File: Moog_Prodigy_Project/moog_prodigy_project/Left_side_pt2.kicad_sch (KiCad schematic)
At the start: 64 parts, among them J7 Conn_01x02_Socket, Q4 BC107, Q7 BC549, SW3 Switch_4x4, SW4 SW_Slide_DPDT_3x3, SW5 Switch_4x4, U2B2 OPA134, U4B1 OPA134, U6 NE5532, U7 AD8066ARM, U8 LT1011CN8

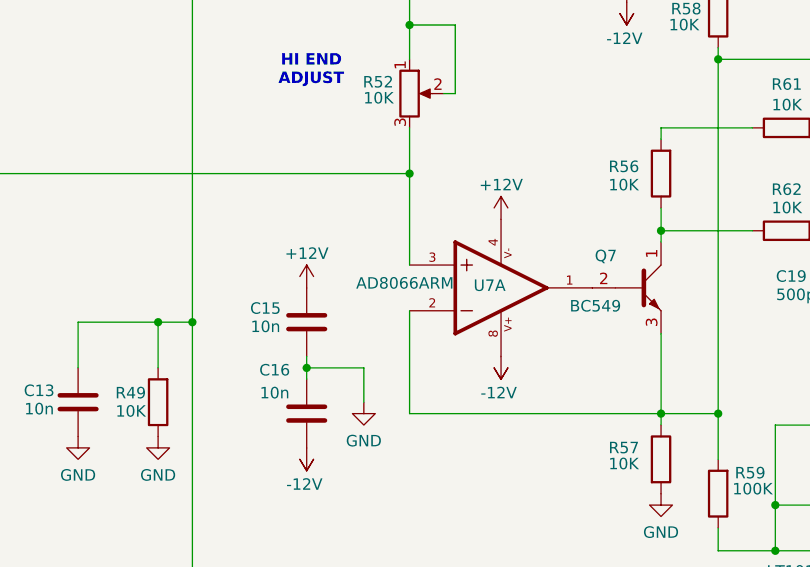
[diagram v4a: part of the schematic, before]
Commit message: SMD component to THT component update PCB
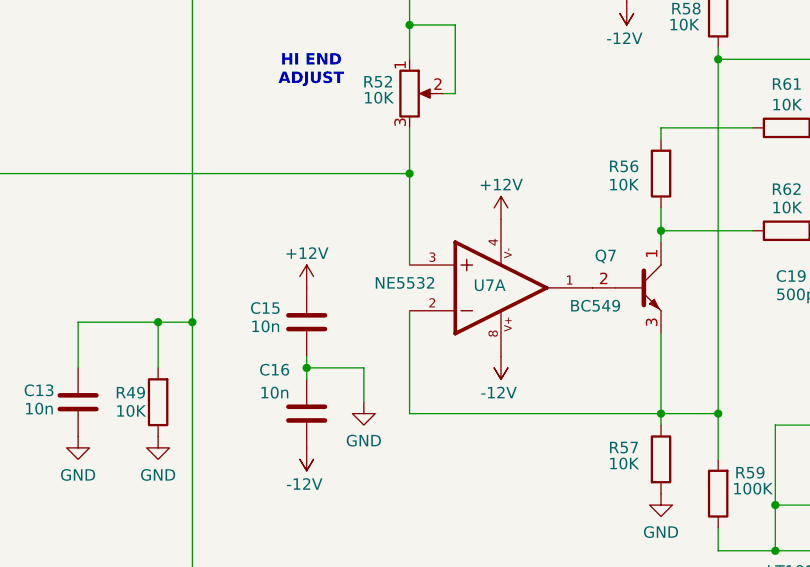
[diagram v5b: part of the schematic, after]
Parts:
- U7: value AD8066ARM -> NE5532; footprint Package_DIP:DIP-8_W7.62mm_Socket -> NE5532AP:DIP794W45P254L1016H508Q8
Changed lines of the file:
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@@
 			)
 		)
-		(property "Value" "AD8066ARM"
+		(property "Value" "NE5532"
 			(at 178.562 104.902 0)
 			(effects
@@
 			)
 		)
-		(property "Footprint" "Package_DIP:DIP-8_W7.62mm_Socket"
+		(property "Footprint" "NE5532AP:DIP794W45P254L1016H508Q8"
 			(at 189.23 105.41 0)
 			(effects

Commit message: Routhed PCB final 17.05.2026
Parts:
- Q5, Q6: footprint BF256C:TO92127P478H483-3 -> Package_TO_SOT_THT:TO-92_Inline
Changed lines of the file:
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@@
 			)
 		)
-		(property "Footprint" "BF256C:TO92127P478H483-3"
+		(property "Footprint" "Package_TO_SOT_THT:TO-92_Inline"
 			(at 184.15 58.42 0)
 			(effects
@@
 			)
 		)
-		(property "Footprint" "BF256C:TO92127P478H483-3"
+		(property "Footprint" "Package_TO_SOT_THT:TO-92_Inline"
 			(at 129.54 33.02 0)
 			(effects

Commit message: Fix 1 nakon review-a 27.05.2026
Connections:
- net +12V: now also CA3046_2.; no longer CA3046_2.8
- net -12V: now also Q4. (E); no longer Q4.1 (E)
- net GND: now also CA3046_2.; no longer CA3046_2.10, CA3046_2.6
- net at R37.2, U4B1.3 (+): now also CA3046_2.; no longer CA3046_2.9
- net at R33.2, R34.2, R35.1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: now also CA3046_2.; no longer CA3046_2.2
- net at C18.1, R54.1, R55.1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: now also Q6.; no longer Q6.2 (G)
- net at R57.1, R58.1, R59.2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: now also Q7. (E), U7.3 (+); no longer Q7.3 (E), U7.2
- net at R40.2, RV8.3: now also CA3046_2.; no longer CA3046_2.4
- net at C17.1, R52.1, R52.2: now also Q5., Q6.; no longer Q5.3 (S), Q6.1 (D)
- net at C17.2, R54.2, U6.1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: now also Q5., Q6.; no longer Q5.1 (D), Q6.3 (S)
- net at SW4.5 (B): now also Q5.; no longer Q5.2 (G)
- net at R56.1, R62.1: now also Q7. (E); no longer Q7.1 (C)
- net at R45.2, R47.2: now also Q4. (E); no longer Q4.2 (B)
- net at R42.2, R44.2: now also CA3046_2.; no longer CA3046_2.13
- net at C12.2, R43.2, SW3.5 (E)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: now also CA3046_2.; no longer CA3046_2.5
- net at U7.1: now also Q7. (E); no longer Q7.2 (B)
- net at R48.1: now also Q4. (E); no longer Q4.3 (C)
- net at R48.2: now also CA3046_2.; no longer CA3046_2.7
- net at C12.1, U2B2.6: now also CA3046_2.; no longer CA3046_2.3
- new net: CA3046_2., R52.3, U7.2 (-)
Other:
- title: (none) -> Drugi segment leve strane šeme
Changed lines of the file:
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@@
 	(generator_version "9.0")
 	(paper "A4")
+	(title_block
+		(title "Drugi segment leve strane šeme")
+		(date "27.05.2026")
+		(rev "Marjan Urekar")
+		(comment 1 "Fakultet tehničkih nauka")
+		(comment 2 "Univerzitet u Novom Sadu")
+		(comment 3 "Merno-Informacioni sistemi")
+		(comment 4 "Jovan Mastelica E1 105/2023")
+	)
 	(text "OSC 2\nFREQ TRIM"
 		(exclude_from_sim no)
@@
 	(wire
 		(pts
+			(xy 179.07 102.87) (xy 181.61 102.87)
+		)
+		(stroke
+			(width 0)
+			(type default)
+		)
+	)
+	(wire
+		(pts
 			(xy 77.47 71.12) (xy 85.09 71.12)
 		)
@@
 	(wire
 		(pts
-			(xy 242.57 137.16) (xy 245.11 137.16)
+			(xy 142.24 109.22) (xy 142.24 114.3)
 		)
 		(stroke
@@
 	(wire
 		(pts
-			(xy 142.24 109.22) (xy 142.24 114.3)
+			(xy 265.43 91.44) (xy 265.43 82.55)
 		)
 		(stroke
@@
 	(wire
 		(pts
-			(xy 265.43 91.44) (xy 265.43 82.55)
+			(xy 48.26 62.23) (xy 48.26 26.67)
 		)
 		(stroke
@@
 	(wire
 		(pts
-			(xy 48.26 62.23) (xy 48.26 26.67)
+			(xy 179.07 107.95) (xy 181.61 107.95)
 		)
 		(stroke
@@
 		(dnp no)
 		(property "Reference" "Q6"
-			(at 183.134 57.912 0)
+			(at 184.404 59.182 0)
 			(effects
 				(font
@@
 			)
 		)
-		(pin "3"
+		(pin ""
 		)
-		(pin "1"
+		(pin ""
 		)
-		(pin "2"
+		(pin ""
 		)
 		(instances
@@
 	)
 	(symbol
+		(lib_name "BF256C_1")
 		(lib_id "Transistor_FET:BF256C")
 		(at 129.54 33.02 0)
@@
 			)
 		)
-		(pin "3"
+		(pin ""
 		)
-		(pin "1"
+		(pin ""
 		)
-		(pin "2"
+		(pin ""
 		)
 		(instances
@@
 		)
 		(property "Value" "LT1011CN8"
-			(at 208.534 66.294 0)
+			(at 208.534 65.786 0)
 			(effects
 				(font
@@
 		(pin "3"
 		)
-		(pin "5"
-		)
 		(pin "2"
 		)
@@
 		(pin "7"
 		)
-		(pin "6"
-		)
 		(pin "8"
 		)
@@
 		)
 		(property "Value" "10K"
-			(at 138.43 163.83 0)
+			(at 139.192 163.83 0)
 			(effects
 				(font
@@
 			)
 		)
-		(pin "9"
+		(pin ""
 		)
-		(pin "11"
+		(pin ""
 		)
-		(pin "14"
+		(pin ""
 		)
-		(pin "13"
+		(pin ""
 		)
-		(pin "6"
+		(pin ""
 		)
-		(pin "7"
+		(pin ""
 		)
-		(pin "12"
+		(pin ""
 		)
-		(pin "10"
+		(pin ""
 		)
-		(pin "8"
+		(pin ""
 		)
-		(pin "1"
+		(pin ""
 		)
-		(pin "5"
+		(pin ""
 		)
-		(pin "3"
+		(pin ""
 		)
-		(pin "2"
+		(pin ""
 		)
-		(pin "4"
+		(pin ""
 		)
 		(instances
@@
 			)
 		)
-		(pin "2"
+		(pin ""
 		)
-		(pin "1"
+		(pin ""
 		)
-		(pin "3"
+		(pin ""
 		)
 		(instances
@@
 		(dnp no)
 		(property "Reference" "U8"
-			(at 233.934 136.906 0)
+			(at 236.982 136.906 0)
 			(effects
 				(font
 					(size 1.27 1.27)
 				)
+				(justify right)
 			)
 		)
 		(property "Value" "LT1011CN8"
-			(at 223.774 136.906 0)
+			(at 229.616 136.906 0)
 			(effects
 				(font
 					(size 1.27 1.27)
 				)
+				(justify right)
 			)
 		)
@@
 		(on_board yes)
 		(dnp no)
-		(fields_autoplaced yes)
 		(property "Reference" "SW5"
-			(at 234.95 58.4199 0)
+			(at 235.458 49.784 0)
 			(effects
 				(font
@@
 		)
 		(property "Value" "Switch_4x4"
-			(at 234.95 60.9599 0)
+			(at 239.522 51.816 0)
 			(effects
 				(font
@@
 			)
 		)
-		(pin "2"
+		(pin ""
 		)
-		(pin "1"
+		(pin ""
 		)
-		(pin "3"
+		(pin ""
 		)
 		(instances

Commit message: Latest checkpoints update 05.06.2026
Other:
- note added: "Promena oktava po položaju preklopnika: 16' - krajnji levi položaj 8' - srednji položaj 4' - krajnji desni položaj"
- note added: "Talasni oblik po položaju preklopnika: Rampa - krajnji levi položaj Trougao - srednji položaj Četvrtke - krajnji desni položaj"
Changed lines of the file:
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@@
 	(text "WAVEFORM\nSELECT"
 		(exclude_from_sim no)
-		(at 242.062 45.466 0)
+		(at 245.618 71.882 0)
 		(effects
 			(font
@@
 		)
 	)
+	(text "Talasni oblik po položaju preklopnika:\nRampa - krajnji levi položaj\nTrougao - srednji položaj\nČetvrtke - krajnji desni položaj\n"
+		(exclude_from_sim no)
+		(at 231.902 43.18 0)
+		(effects
+			(font
+				(size 1.27 1.27)
+			)
+			(justify left)
+		)
+	)
 	(text "INTERVAL"
 		(exclude_from_sim no)
@@
 		)
 	)
+	(text "Promena oktava po položaju preklopnika:\n16' - krajnji levi položaj \n8' - srednji položaj \n4' - krajnji desni položaj \n"
+		(exclude_from_sim no)
+		(at 55.88 26.924 0)
+		(effects
+			(font
+				(size 1.27 1.27)
+			)
+			(justify left)
+		)
+	)
 	(text "HI END \nADJUST"
 		(exclude_from_sim no)
@@
 	(wire
 		(pts
-			(xy 190.5 72.39) (xy 190.5 34.29)
+			(xy 190.5 72.39) (xy 190.5 27.94)
 		)
 		(stroke
@@
 	(wire
 		(pts
-			(xy 265.43 91.44) (xy 265.43 82.55)
-		)
-		(stroke
-			(width 0)
-			(type default)
-		)
-	)
-	(wire
-		(pts
-			(xy 48.26 62.23) (xy 48.26 26.67)
+			(xy 48.26 62.23) (xy 48.26 20.32)
 		)
 		(stroke
@@
 	(wire
 		(pts
-			(xy 48.26 26.67) (xy 107.95 26.67)
+			(xy 48.26 20.32) (xy 107.95 20.32)
 		)
 		(stroke
@@
 	(wire
 		(pts
-			(xy 236.22 64.77) (xy 236.22 80.01)
+			(xy 232.41 68.58) (xy 232.41 80.01)
 		)
 		(stroke
@@
 	(wire
 		(pts
-			(xy 262.89 91.44) (xy 265.43 91.44)
+			(xy 262.89 91.44) (xy 266.7 91.44)
 		)
 		(stroke
@@
 	(wire
 		(pts
-			(xy 190.5 34.29) (xy 205.74 34.29)
+			(xy 190.5 27.94) (xy 205.74 27.94)
 		)
 		(stroke
@@
 	(wire
 		(pts
-			(xy 107.95 26.67) (xy 107.95 92.71)
+			(xy 107.95 20.32) (xy 107.95 92.71)
 		)
 		(stroke
@@
 	(wire
 		(pts
+			(xy 232.41 68.58) (xy 236.22 68.58)
+		)
+		(stroke
+			(width 0)
+			(type default)
+		)
+	)
+	(wire
+		(pts
 			(xy 208.28 52.07) (xy 213.36 52.07)
 		)
@@
 	(wire
 		(pts
+			(xy 236.22 68.58) (xy 236.22 64.77)
+		)
+		(stroke
+			(width 0)
+			(type default)
+		)
+	)
+	(wire
+		(pts
 			(xy 158.75 152.4) (xy 152.4 152.4)
 		)
@@
 	(wire
 		(pts
-			(xy 213.36 80.01) (xy 236.22 80.01)
+			(xy 213.36 80.01) (xy 232.41 80.01)
 		)
 		(stroke
@@
 	(global_label "Ulaz_na_diodnu_zastitu"
 		(shape input)
-		(at 205.74 34.29 0)
+		(at 205.74 27.94 0)
 		(fields_autoplaced yes)
 		(effects
@@
 		)
 		(property "Intersheetrefs" "${INTERSHEET_REFS}"
-			(at 230.859 34.29 0)
+			(at 230.859 27.94 0)
 			(effects
 				(font
@@
 	(global_label "Flag_ka_R94"
 		(shape input)
-		(at 265.43 82.55 90)
+		(at 266.7 91.44 0)
 		(fields_autoplaced yes)
 		(effects
@@
 		)
 		(property "Intersheetrefs" "${INTERSHEET_REFS}"
-			(at 265.43 67.7117 90)
+			(at 281.5383 91.44 0)
 			(effects
 				(font
@@
 		)
 		(property "Value" "10K"
-			(at 258.064 92.71 0)
+			(at 257.048 92.202 0)
 			(effects
 				(font
@@
 		(dnp no)
 		(property "Reference" "R64"
-			(at 240.538 83.82 90)
+			(at 236.728 78.232 90)
 			(effects
 				(font
@@
 		)
 		(property "Value" "10K"
-			(at 240.538 85.598 90)
+			(at 236.474 80.264 90)
 			(effects
 				(font
@@
 	)
 	(symbol
+		(lib_name "SW_Slide_DPDT_4x4_1")
 		(lib_id "Power_supply:SW_Slide_DPDT_4x4")
 		(at 78.74 36.83 0)
@@
 		(on_board yes)
 		(dnp no)
-		(fields_autoplaced yes)
 		(property "Reference" "SW3"
-			(at 69.85 36.8299 0)
+			(at 91.694 34.29 0)
 			(effects
 				(font
@@
 		)
 		(property "Value" "Switch_4x4"
-			(at 69.85 39.3699 0)
+			(at 88.138 38.1 0)
 			(effects
 				(font
@@
 		(dnp no)
 		(property "Reference" "SW5"
-			(at 235.458 49.784 0)
+			(at 240.284 52.07 0)
 			(effects
 				(font
@@
 		)
 		(property "Value" "Switch_4x4"
-			(at 239.522 51.816 0)
+			(at 252.73 50.292 0)
 			(effects
 				(font
@@
 				)
 				(justify right)
+				(hide yes)
 			)
 		)
@@
 		(dnp no)
 		(property "Reference" "C19"
-			(at 221.488 104.14 0)
+			(at 222.25 104.902 0)
 			(effects
 				(font
@@
 		)
 		(property "Value" "500p"
-			(at 221.996 106.172 0)
+			(at 222.758 106.934 0)
 			(effects
 				(font
